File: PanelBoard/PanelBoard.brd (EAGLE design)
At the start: 20.3 x 25.1 mm, 4 parts, among them K1 ARK500/3

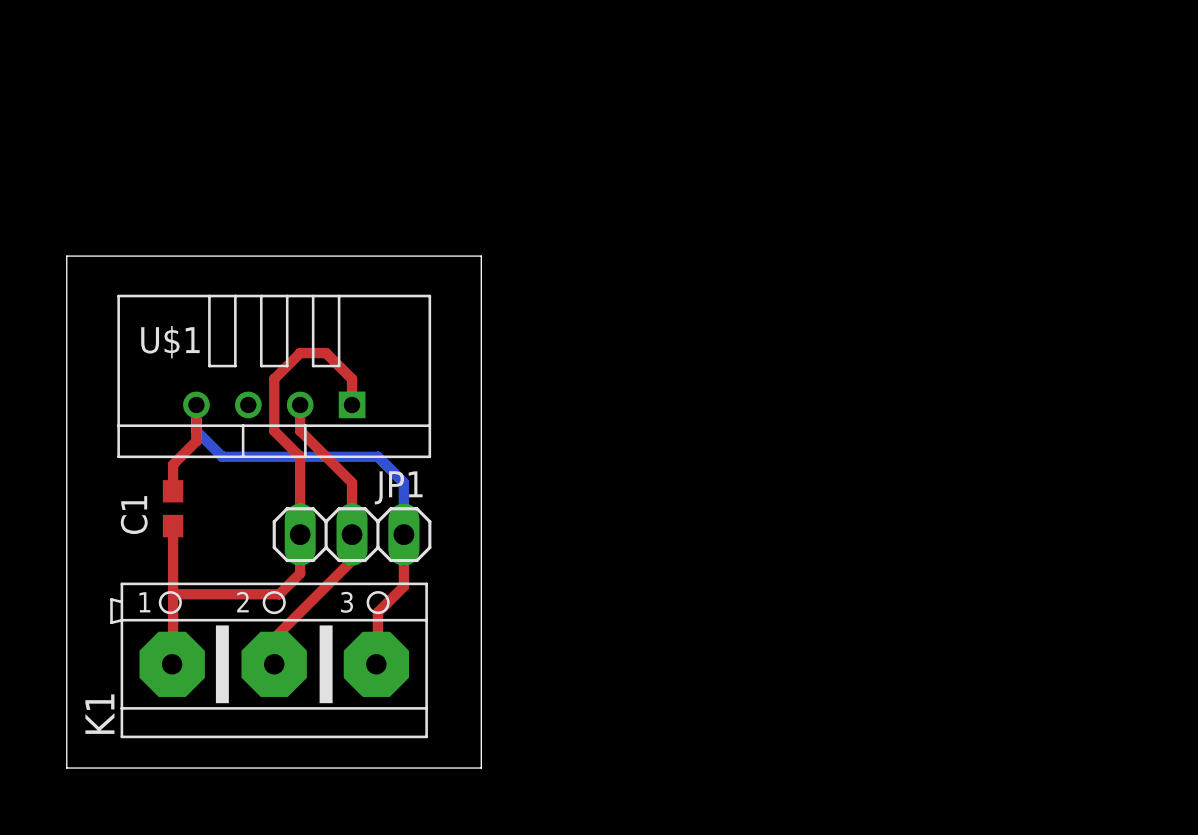
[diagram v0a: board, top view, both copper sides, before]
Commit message: Add PanelBoard
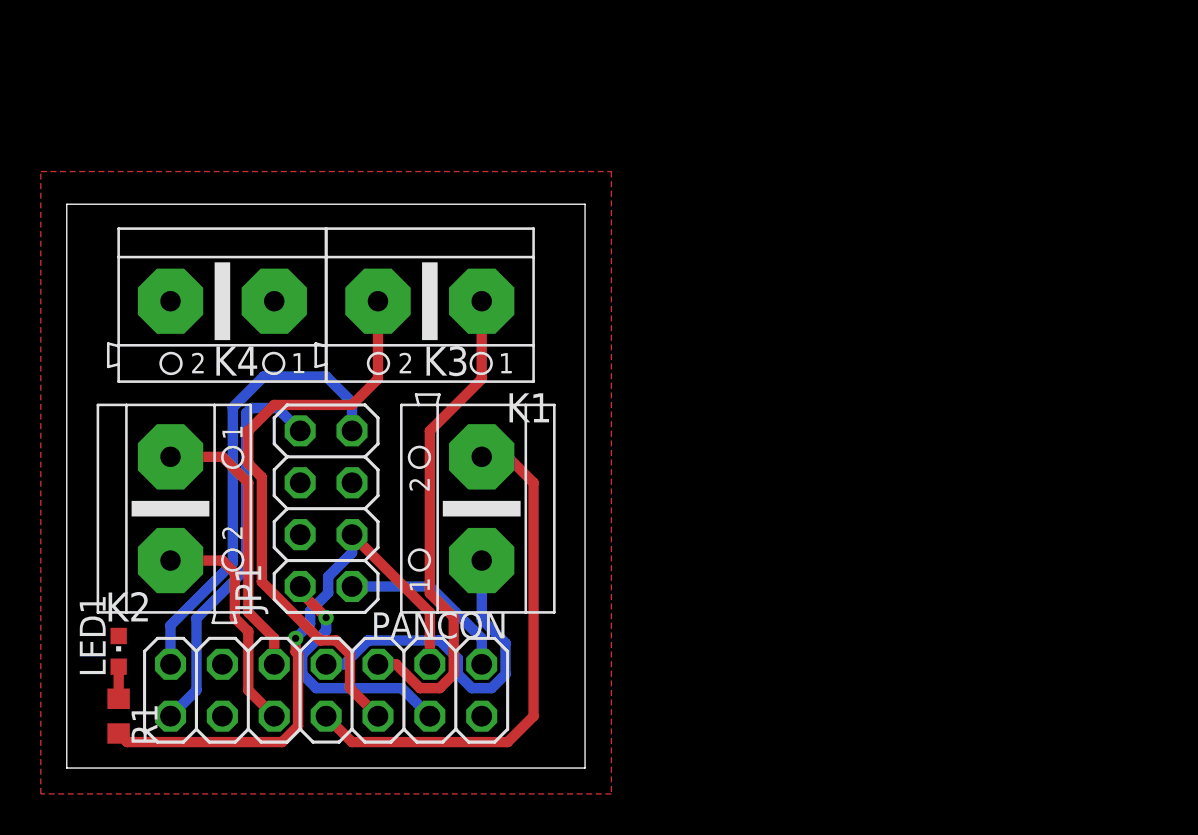
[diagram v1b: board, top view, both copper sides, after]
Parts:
- removed C1: 100nF, rcl:C0603
- removed U$1: DHT22, diy-modules:TEMP-HUM-SENSOR-DHT22
- added K2, K3, K4: ARK500/2, #PaJa_konektory:ARK500/2
- added LED1: (no value), led:CHIPLED_0603
- added PANCON: (no value), pinhead:2X07
- added R1: (no value), rcl:R0603
- JP1: device pinhead:1X03 -> pinhead:2X04
- K1: value ARK500/3 -> ARK500/2; device #PaJa_konektory:ARK500/3 -> #PaJa_konektory:ARK500/2
- moved K1 12.7 mm to (20.3, 12.7), turned to 90 degrees
- moved JP1 1.80 mm to (12.7, 12.7), turned to 90 degrees
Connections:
- removed net DATA_OUT: JP1.2, K1.2, U$1.2
- new net +3V3: JP1.3, PANCON.3, R1.2
- new net B_BACKSPACE: K2.2, PANCON.10
- new net B_DOWN: K1.2, PANCON.8
- new net B_ENTER: K2.1, PANCON.9
- new net B_UP: K1.1, PANCON.7
- new net I2C_SCL: JP1.7, PANCON.13
- new net I2C_SDA: JP1.8, PANCON.14
- new net MP1: K4.1
- new net MP2: K4.2
- new net N$1: JP1.5
- new net N$2: JP1.6
- new net N$4: LED1.A, R1.1
- new net N$8: PANCON.11
- new net N$9: PANCON.12
- new net S_CLOSE: K3.2, PANCON.6
- new net S_OPEN: K3.1, PANCON.5
- net +5V: now also PANCON.1; no longer C1.2, K1.1, U$1.1
- net GND: now also JP1.2, JP1.4, LED1.C, PANCON.2, PANCON.4; no longer C1.1, JP1.3, K1.3, U$1.4
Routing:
- net S_CLOSE: track 0.00 -> 28.3 mm
- net +3V3: track 0.00 -> 27.8 mm, vias 0 -> 1
- net B_DOWN: track 0.00 -> 25.7 mm
- net S_OPEN: track 0.00 -> 24.3 mm
- net I2C_SCL: track 0.00 -> 22.2 mm
- net +5V: track 29.6 -> 8.67 mm
- net I2C_SDA: track 0.00 -> 19.6 mm
- net B_UP: track 0.00 -> 17.0 mm
- net DATA_OUT: track 15.3 -> 0.00 mm
- net GND: track 26.6 -> 12.4 mm, vias 0 -> 1
- net B_ENTER: track 0.00 -> 13.8 mm
- net B_BACKSPACE: track 0.00 -> 11.2 mm
- net N$4: track 0.00 -> 1.57 mm
- added copper zone on layer 1, net GND
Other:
- board size 20.3 x 25.1 mm -> 25.4 x 27.6 mm
- board text removed: "PPSB-TH v1.0"
- board text removed: "PROTOPlant"
- board text removed: "designed by PS"

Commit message: PanelBoard layout reworked
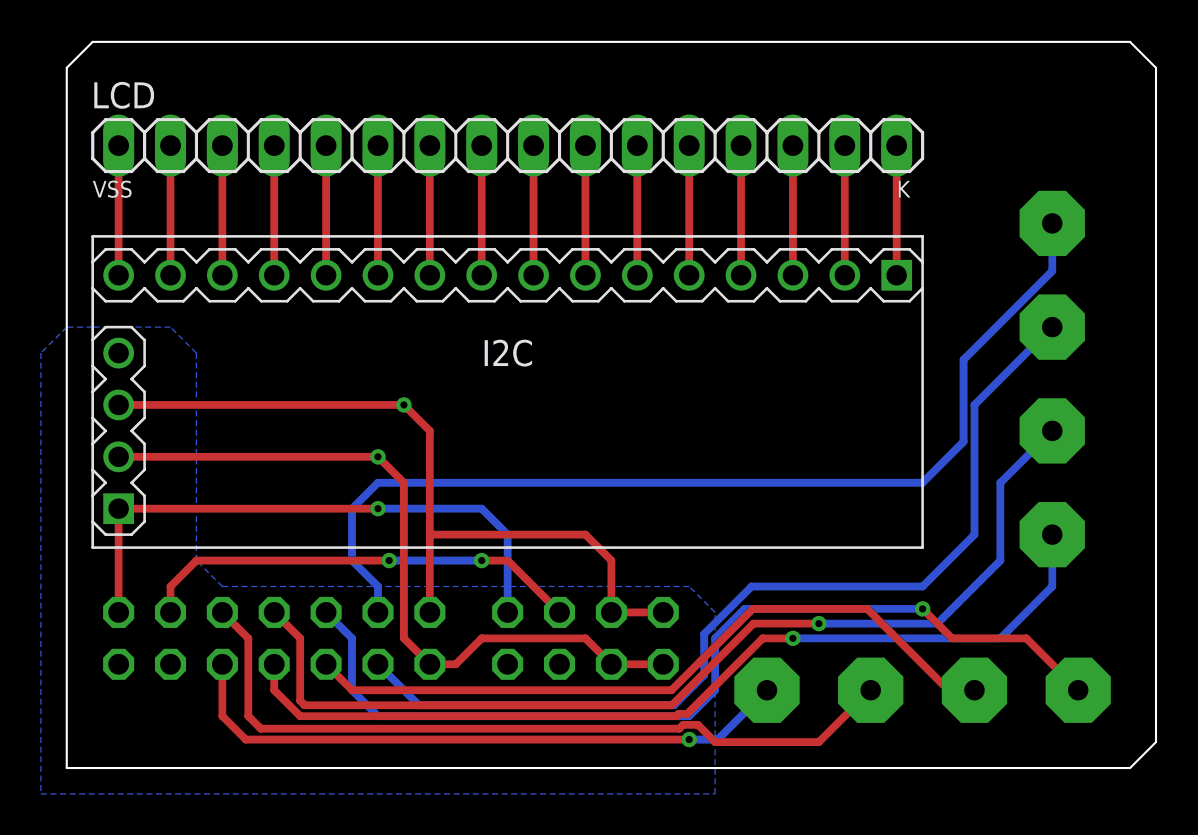
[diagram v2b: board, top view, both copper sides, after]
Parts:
- removed LED1: (no value), led:CHIPLED_0603
- removed R1: (no value), rcl:R0603
- added I2C: LCD-I2C-CONVERTER, diy-modules:LCD-I2C-CONVERTER
- added LCD: (no value), pinhead:1X16
- JP1: device pinhead:2X04 -> pinhead:2X04/90
- PANCON: device pinhead:2X07 -> pinhead:2X07/90
- moved K2 42.8 mm to (47.0, 3.81), flipped to the bottom, turned to 0 degrees
- moved K4 40.7 mm to (48.3, 24.1), flipped to the bottom, turned to 270 degrees
- moved K1 28.0 mm to (48.3, 14.0), flipped to the bottom, turned to 270 degrees
- moved K3 26.9 mm to (36.8, 3.81), flipped to the bottom, turned to 0 degrees
- moved JP1 17.1 mm to (25.4, 1.27), flipped to the bottom, turned to 180 degrees
- moved PANCON 3.59 mm to (10.2, 1.27), flipped to the bottom
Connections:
- removed net N$1: JP1.5
- removed net N$2: JP1.6
- removed net N$4: LED1.A, R1.1
- removed net N$8: PANCON.11
- removed net N$9: PANCON.12
- new net N$10: I2C.J2.12, LCD.5
- new net N$11: I2C.J2.11, LCD.6
- new net N$12: I2C.J2.10, LCD.7
- new net N$13: I2C.J2.9, LCD.8
- new net N$14: I2C.J2.8, LCD.9
- new net N$15: I2C.J2.7, LCD.10
- new net N$16: I2C.J2.6, LCD.11
- new net N$17: I2C.J2.5, LCD.12
- new net N$18: I2C.J2.4, LCD.13
- new net N$19: I2C.J2.3, LCD.14
- new net N$20: I2C.J2.2, LCD.15
- new net N$21: I2C.J2.1, LCD.16
- new net N$3: I2C.J2.16, LCD.1
- new net N$5: I2C.J2.15, LCD.2
- new net N$6: I2C.J2.14, LCD.3
- new net N$7: I2C.J2.13, LCD.4
- net +3V3: no longer R1.2
- net +5V: now also I2C.J1.1
- net GND: now also I2C.J1.4; no longer LED1.C
- net I2C_SCL: now also I2C.J1.3, JP1.5
- net I2C_SDA: now also I2C.J1.2, JP1.6
- net MP1: now also PANCON.11
- net MP2: now also PANCON.12
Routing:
- net MP1: track 0.00 -> 49.4 mm
- net MP2: track 0.00 -> 46.4 mm
- net B_UP: track 17.0 -> 49.6 mm, vias 0 -> 1
- net B_ENTER: track 13.8 -> 45.7 mm, vias 0 -> 1
- net B_BACKSPACE: track 11.2 -> 35.6 mm
- net +5V: track 8.67 -> 28.5 mm, vias 0 -> 1
- net B_DOWN: track 25.7 -> 45.1 mm, vias 0 -> 1
- net I2C_SCL: track 22.2 -> 39.2 mm, vias 0 -> 1
- net I2C_SDA: track 19.6 -> 36.4 mm, vias 0 -> 1
- net S_OPEN: track 24.3 -> 37.8 mm
- net GND: track 12.4 -> 0.00 mm, vias 1 -> 0
- net N$7: track 0.00 -> 6.35 mm
- net N$6: track 0.00 -> 6.35 mm
- net N$5: track 0.00 -> 6.35 mm
- net N$3: track 0.00 -> 6.35 mm
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- added copper zone on layer 16, net GND
- removed copper zone on layer 1, net GND
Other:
- board size 25.4 x 27.6 mm -> 53.3 x 35.6 mm
- board text added: "1"
- board text added: "14"
- board text added: "16"
- board text added: "K"
- board text added: "PROTOPlant PanelBoard"
- board text added: "Petr Stourac 2020"
- board text added: "VSS"

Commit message: Improved schematics layout.
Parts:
- moved K1 1.27 mm to (49.5, 14.0)
- moved K4 1.27 mm to (49.5, 24.1)
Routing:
- net MP1: track 49.4 -> 49.9 mm
- net MP2: track 46.4 -> 47.0 mm
- net B_UP: track 49.6 -> 50.1 mm
- net B_DOWN: track 45.1 -> 45.6 mm
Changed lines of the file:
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@@
 <drawing>
 <settings>
-<setting alwaysvectorfont="yes"/>
+<setting alwaysvectorfont="no"/>
 <setting verticaltext="up"/>
 </settings>
@@
 </layers>
 <board>
-<fusionsync huburn="a.cGVyc29uYWw6dWUyYzQ3NTBk" projecturn="a.cGVyc29uYWw6dWUyYzQ3NTBkIzIwMjAwMjE0MjY1NTk3Mjc2" f3durn="urn:adsk.wipprod:dm.lineage:b-HqdqnqQIujW4GbYgv2IA" pcbguid="b09f9af9-6d01-48f4-b537-68b3158d0bda" lastpulledtime="2020-04-18T11:30:07Z" lastsyncedchangeguid="e40187d6-1b40-b4d3-6492-74cde82d2f4a" latestrevisionid="" lastsyncedrevisionid="" lastboardhashguid="5d1565bc-5885-4c87-dfc4-e1cb402c18c1" lastpushedtime="2020-04-18T12:57:09Z" linktopcb3d="%12"/>
+<fusionsync huburn="a.YnVzaW5lc3M6Z21haWw4Mzc2MTI" projecturn="a.YnVzaW5lc3M6Z21haWw4Mzc2MTIjMjAyMDA1MDEyOTMzMTU4NTE" f3durn="urn:adsk.wipprod:dm.lineage:mOQNbksbRLagO3vyteS2RA" pcbguid="22918768-c7d9-4666-837f-f2fe6027da72" lastpulledtime="" lastsyncedchangeguid="aebcccfe-9973-5294-3423-f0e43b8a8434" latestrevisionid="2570a0e5-c5e6-409a-a5d2-18f75b015ca8" lastsyncedrevisionid="2570a0e5-c5e6-409a-a5d2-18f75b015ca8" lastboardhashguid="98bd4875-e8e5-4f82-1001-d87223a06b32" lastpushedtime="2020-05-02T01:38:35Z" linktopcb3d="%12"/>
 <plain>
 <text x="52.07" y="33.02" size="1.778" layer="26" rot="MR0">PROTOPlant PanelBoard</text>
@@
 <text x="1.27" y="7.62" size="1.27" layer="26" rot="MR0">1</text>
 <text x="20.32" y="4.572" size="1.27" layer="26" rot="MR0">14</text>
+<text x="1.27" y="27.94" size="0.8128" layer="25">VSS</text>
+<text x="40.64" y="27.94" size="0.8128" layer="25">K</text>
 <wire x1="0" y1="0" x2="52.07" y2="0" width="0.1016" layer="20"/>
 <wire x1="52.07" y1="0" x2="53.34" y2="1.27" width="0.1016" layer="20"/>
@@
 <wire x1="1.27" y1="35.56" x2="0" y2="34.29" width="0.1016" layer="20"/>
 <wire x1="0" y1="34.29" x2="0" y2="0" width="0.1016" layer="20"/>
-<text x="1.27" y="27.94" size="0.8128" layer="25">VSS</text>
-<text x="40.64" y="27.94" size="0.8128" layer="25">K</text>
 </plain>
 <attributes>
@@
 <attribute name="VALUE" x="20.32" y="5.715" size="1.27" layer="28" rot="MR180"/>
 </element>
-<element name="K1" library="#PaJa_konektory" package="ARK500/2" value="ARK500/2" x="48.26" y="13.97" smashed="yes" rot="MR270">
-<attribute name="NAME" x="43.498" y="12.855" size="1.4224" layer="26" rot="MR270"/>
-<attribute name="VALUE" x="51.59" y="18.6793" size="1.016" layer="28" rot="MR270"/>
-</element>
-<element name="K2" library="#PaJa_konektory" package="ARK500/2" value="ARK500/2" x="46.99" y="3.81" smashed="yes" rot="MR0">
+<element name="K1" library="#PaJa_konektory" library_urn="urn:adsk.eagle:library:19754563" package="ARK500/2" package3d_urn="urn:adsk.eagle:package:19754484/4" value="ARK500/2" x="49.53" y="13.97" smashed="yes" rot="MR270">
+<attribute name="NAME" x="44.768" y="12.855" size="1.4224" layer="26" rot="MR270"/>
+<attribute name="VALUE" x="52.86" y="18.6793" size="1.016" layer="28" rot="MR270"/>
+</element>
+<element name="K2" library="#PaJa_konektory" library_urn="urn:adsk.eagle:library:19754563" package="ARK500/2" package3d_urn="urn:adsk.eagle:package:19754484/4" value="ARK500/2" x="46.99" y="3.81" smashed="yes" rot="MR0">
 <attribute name="NAME" x="44.351" y="8.191" size="1.4224" layer="26" rot="MR0"/>
 <attribute name="VALUE" x="51.6993" y="0.48" size="1.016" layer="28" rot="MR0"/>
 </element>
-<element name="K3" library="#PaJa_konektory" package="ARK500/2" value="ARK500/2" x="36.83" y="3.81" smashed="yes" rot="MR0">
+<element name="K3" library="#PaJa_konektory" library_urn="urn:adsk.eagle:library:19754563" package="ARK500/2" package3d_urn="urn:adsk.eagle:package:19754484/4" value="ARK500/2" x="36.83" y="3.81" smashed="yes" rot="MR0">
 <attribute name="NAME" x="34.318" y="8.191" size="1.4224" layer="26" rot="MR0"/>
 <attribute name="VALUE" x="41.5393" y="0.48" size="1.016" layer="28" rot="MR0"/>
 </element>
-<element name="K4" library="#PaJa_konektory" package="ARK500/2" value="ARK500/2" x="48.26" y="24.13" smashed="yes" rot="MR270">
-<attribute name="NAME" x="43.498" y="21.745" size="1.4224" layer="26" rot="MR270"/>
-<attribute name="VALUE" x="51.59" y="28.8393" size="1.016" layer="28" rot="MR270"/>
+<element name="K4" library="#PaJa_konektory" library_urn="urn:adsk.eagle:library:19754563" package="ARK500/2" package3d_urn="urn:adsk.eagle:package:19754484/4" value="ARK500/2" x="49.53" y="24.13" smashed="yes" rot="MR270">
+<attribute name="NAME" x="44.768" y="21.745" size="1.4224" layer="26" rot="MR270"/>
+<attribute name="VALUE" x="52.86" y="28.8393" size="1.016" layer="28" rot="MR270"/>
 </element>
 <element name="LCD" library="pinhead" library_urn="urn:adsk.eagle:library:325" package="1X16" package3d_urn="urn:adsk.eagle:package:22432/2" value="" x="21.59" y="30.48" smashed="yes">
@@
 <wire x1="33.62841875" y1="7.0711" x2="36.83" y2="7.0711" width="0.381" layer="1"/>
 <wire x1="36.83" y1="7.0711" x2="42.6311" y2="7.0711" width="0.381" layer="16"/>
-<wire x1="45.72" y1="13.97" x2="48.26" y2="16.51" width="0.381" layer="16"/>
+<wire x1="45.72" y1="12.7" x2="49.53" y2="16.51" width="0.381" layer="16"/>
 <wire x1="42.6311" y1="7.0711" x2="45.72" y2="10.16" width="0.381" layer="16"/>
-<wire x1="45.72" y1="10.16" x2="45.72" y2="13.97" width="0.381" layer="16"/>
+<wire x1="45.72" y1="10.16" x2="45.72" y2="12.7" width="0.381" layer="16"/>
 </signal>
 <signal name="B_DOWN">
@@
 <via x="35.56" y="6.35" extent="1-16" drill="0.35"/>
 <wire x1="35.56" y1="6.35" x2="45.72" y2="6.35" width="0.381" layer="16"/>
-<wire x1="45.72" y1="6.35" x2="48.26" y2="8.89" width="0.381" layer="16"/>
-<wire x1="48.26" y1="8.89" x2="48.26" y2="11.43" width="0.381" layer="16"/>
+<wire x1="45.72" y1="6.35" x2="49.53" y2="10.16" width="0.381" layer="16"/>
+<wire x1="49.53" y1="10.16" x2="49.53" y2="11.43" width="0.381" layer="16"/>
 <wire x1="11.43" y1="2.54" x2="29.8516625" y2="2.54" width="0.381" layer="1"/>
 <wire x1="30.38101875" y1="2.6487" x2="34.08231875" y2="6.35" width="0.381" layer="1"/>
@@
 <wire x1="15.24" y1="13.97" x2="41.91" y2="13.97" width="0.381" layer="16"/>
 <wire x1="41.91" y1="13.97" x2="43.9166" y2="15.9766" width="0.381" layer="16"/>
-<wire x1="48.26" y1="24.33768125" x2="48.26" y2="26.67" width="0.381" layer="16"/>
+<wire x1="49.53" y1="25.60768125" x2="49.53" y2="26.67" width="0.381" layer="16"/>
 <wire x1="43.9166" y1="15.9766" x2="43.9166" y2="19.99428125" width="0.381" layer="16"/>
-<wire x1="43.9166" y1="19.99428125" x2="48.26" y2="24.33768125" width="0.381" layer="16"/>
+<wire x1="43.9166" y1="19.99428125" x2="49.53" y2="25.60768125" width="0.381" layer="16"/>
 </signal>
 <signal name="MP2">
@@
 <wire x1="31.2166" y1="6.57094375" x2="33.53565625" y2="8.89" width="0.381" layer="16"/>
 <wire x1="41.91" y1="8.89" x2="44.45" y2="11.43" width="0.381" layer="16"/>
-<wire x1="44.45" y1="11.43" x2="44.45" y2="17.78" width="0.381" layer="16"/>
-<wire x1="44.45" y1="17.78" x2="48.26" y2="21.59" width="0.381" layer="16"/>
+<wire x1="44.45" y1="11.43" x2="44.45" y2="16.51" width="0.381" layer="16"/>
+<wire x1="44.45" y1="16.51" x2="49.53" y2="21.59" width="0.381" layer="16"/>
 <wire x1="17.2466" y1="3.0734" x2="29.7434" y2="3.0734" width="0.381" layer="16"/>
 <wire x1="29.7434" y1="3.0734" x2="31.2166" y2="4.5466" width="0.381" layer="16"/>
